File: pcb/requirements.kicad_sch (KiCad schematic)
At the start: 13 parts

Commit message: Updated symbol with new designator
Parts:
- renumbered S1 to SYM1, S2 to SYM2, S3 to SYM3, S4 to SYM4
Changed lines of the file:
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@@
 		(dnp no)
 		(fields_autoplaced yes)
-		(property "Reference" "S3"
+		(property "Reference" "SYM3"
 			(at 102.87 196.088 0)
 			(effects
@@
 			(project "current-module"
 				(path "/a8149920-3b7f-4d7d-8e96-7a0b38870225/286c1f37-b285-4c3f-bd6d-061a220fab98"
-					(reference "S3")
+					(reference "SYM3")
 					(unit 1)
 				)
@@
 		(dnp no)
 		(fields_autoplaced yes)
-		(property "Reference" "S4"
+		(property "Reference" "SYM4"
 			(at 114.3 196.088 0)
 			(effects
@@
 			(project "current-module"
 				(path "/a8149920-3b7f-4d7d-8e96-7a0b38870225/286c1f37-b285-4c3f-bd6d-061a220fab98"
-					(reference "S4")
+					(reference "SYM4")
 					(unit 1)
 				)
@@
 		(dnp no)
 		(fields_autoplaced yes)
-		(property "Reference" "S1"
+		(property "Reference" "SYM1"
 			(at 80.01 196.088 0)
 			(effects
@@
 			(project "current-module"
 				(path "/a8149920-3b7f-4d7d-8e96-7a0b38870225/286c1f37-b285-4c3f-bd6d-061a220fab98"
-					(reference "S1")
+					(reference "SYM1")
 					(unit 1)
 				)
@@
 		(dnp no)
 		(fields_autoplaced yes)
-		(property "Reference" "S2"
+		(property "Reference" "SYM2"
 			(at 91.44 196.088 0)
 			(effects
@@
 			(project "current-module"
 				(path "/a8149920-3b7f-4d7d-8e96-7a0b38870225/286c1f37-b285-4c3f-bd6d-061a220fab98"
-					(reference "S2")
-					(unit 1)
-				)
+					(reference "SYM2")
+					(unit 1)
+				)

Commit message: Redesign with MCU
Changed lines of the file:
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@@
 		)
 	)
-	(text_box "Interfaces:\n* 1 - Analog Out\n* AC Sense"
+	(text_box "Interfaces:\n* 2 - QWICC\n* 2 - Power\n* UDPI"
 		(exclude_from_sim yes)
 		(at 189.992 25.4 0)
@@
 		)
 	)
-	(text_box "BASIC\n\n* Detect AC current up to 30A\n* Adjustable gain/sensitivity\n* VOUT proportional to current\n* Linear analog output 0 - 3.3VDC\n* Direct AC connect or through cable\n* Cable - 10/3 SJTW Max"
+	(text_box "BASIC\n\n* Detect AC current up to 30A\n* Adjustable gain/sensitivity\n* VOUT proportional to current\n* Linear analog output 0 - 3.3VDC\n* Direct AC connect or through cable\n* Seesaw Module"
 		(exclude_from_sim yes)
 		(at 17.78 25.4 0)

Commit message: Clean up, arranging, ERC and DCR
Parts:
- added LOGO6: ~, CRGM Logos:Aquarius Logo 5mm, symbol CRGM Logos:Aquarius Logo
- LOGO2: footprint CRGM Logos:Roxy 5mm -> CRGM Logos:Roxy 3.5mm

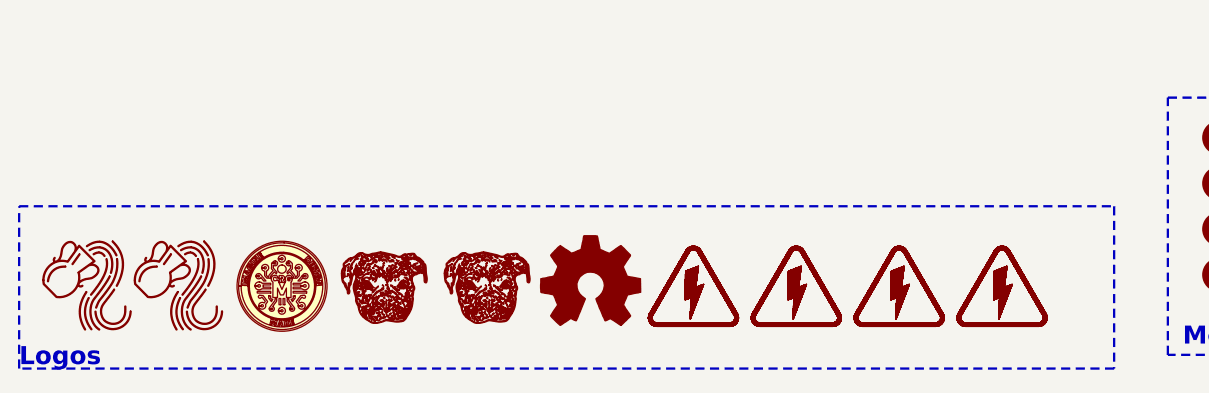
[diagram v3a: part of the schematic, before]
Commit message: Tightened to 50mm wide
SO MUCH fiddling!
Changed I2C to single jumpers
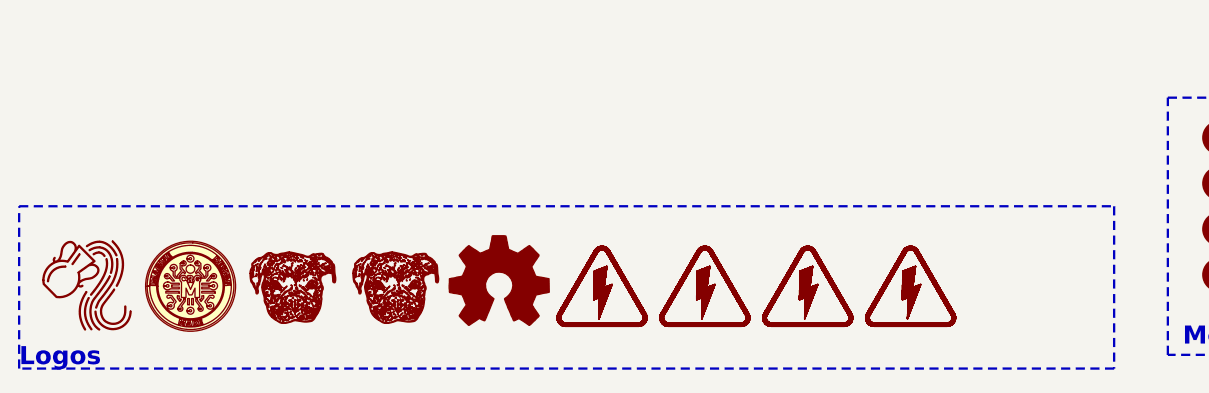
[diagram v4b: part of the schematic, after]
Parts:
- removed LOGO6: ~, CRGM Logos:Aquarius Logo 5mm, symbol CRGM Logos:Aquarius Logo

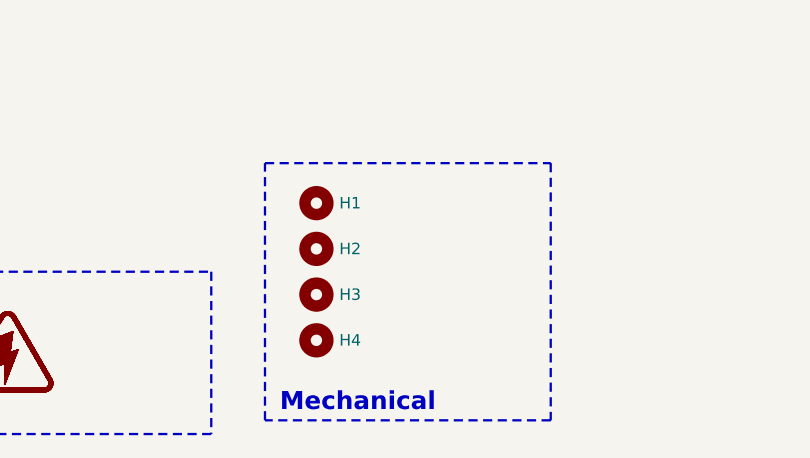
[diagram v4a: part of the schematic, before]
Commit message: Updates for consistency
Changed mounting holes to grounded
Updated power connectors
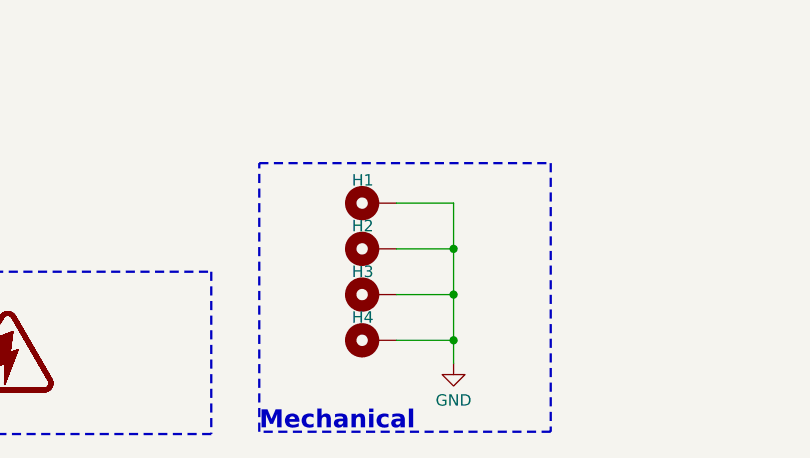
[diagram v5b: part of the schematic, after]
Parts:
- H1, H2, H3, H4: symbol Mechanical:MountingHole -> CRGM Mechanical:MountingHole_Pad
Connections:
- new net GND: H1.1, H2.1, H3.1, H4.1

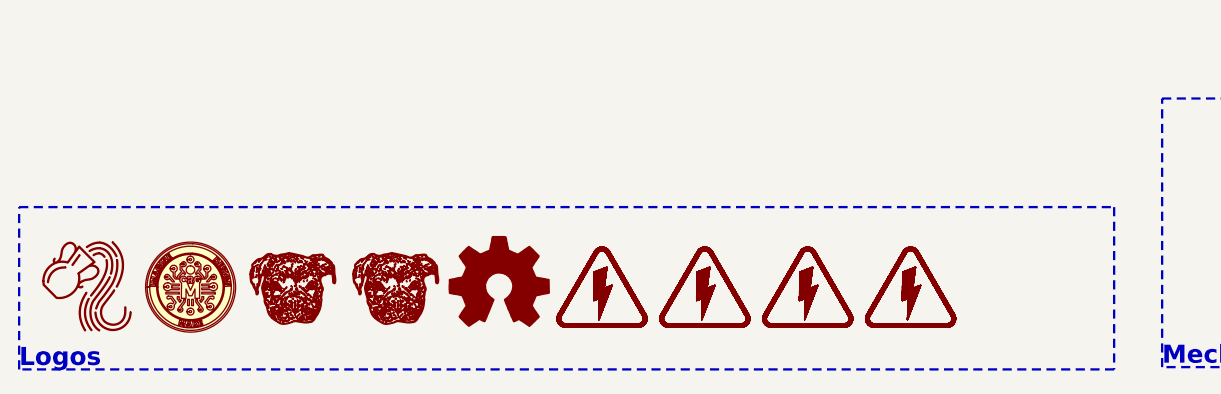
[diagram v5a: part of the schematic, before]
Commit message: Added FNWW to silkscreen
Updated renders on schematics
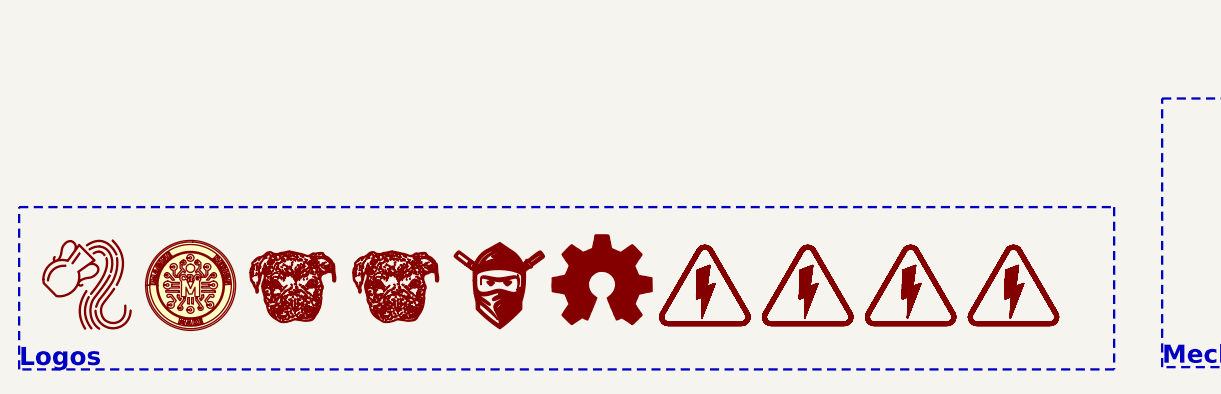
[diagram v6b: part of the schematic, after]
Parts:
- added LOGO6: ~, CRGM Logos:FNWW Face 5mm, symbol CRGM Logos:FNWW Face
